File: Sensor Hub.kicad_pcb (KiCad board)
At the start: 4 copper layers, 52.1 x 45.6 mm, 53 parts, among them J1 SWD, J2 SD_Card, J4 USB_B_Micro, Q1 AO3401A, Q2 AO3401A, SW1 SW_SPDT, SW2 SW_Push, U1 LM20BIM7, U2 STM32L100RBT6A_LQFP64, U3 LD_SSOP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

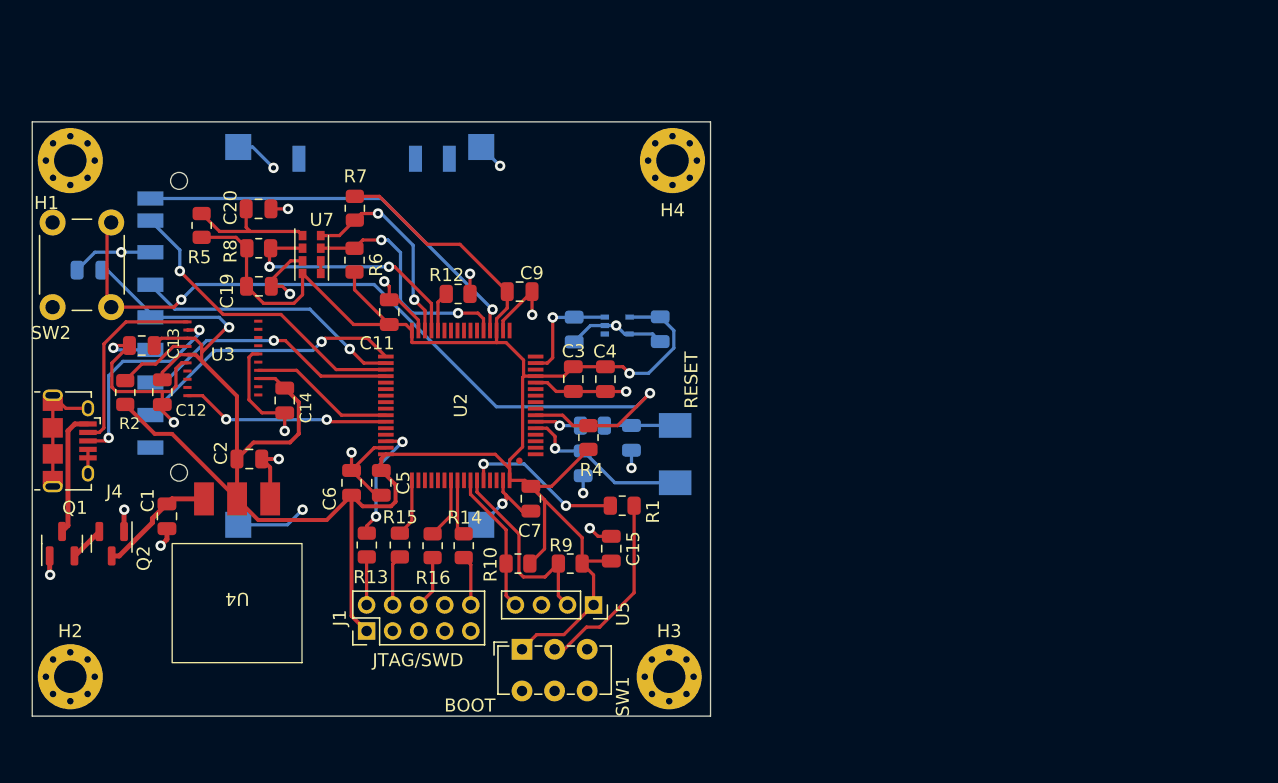
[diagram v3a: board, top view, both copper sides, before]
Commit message: Updated to Rev B
+ Added ESD protection on USB side
+ Redesigned board layout to a SIG/GND/GND/SIG stack up and using L4 as 3V3 plane
+ Resized capacitors and resistors to 0402
+ Added 3D models of certain components
+ Added ferrite bead to 5V line
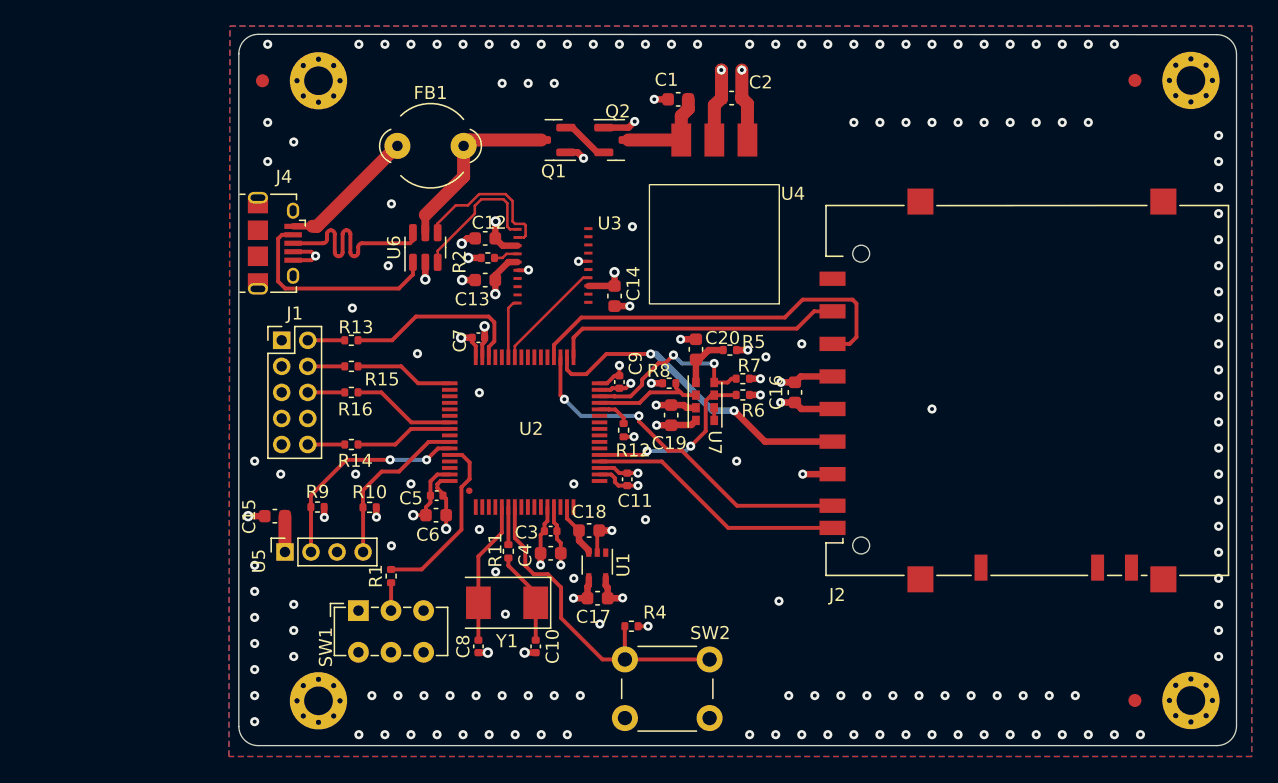
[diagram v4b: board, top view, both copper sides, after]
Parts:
- added FB1: FerriteBead, Ferrite_THT:LairdTech_28C0236-0JW-10, F.Cu at (79.0, 57.8)
- added FID1: Fiducial, Fiducial:Fiducial_1mm_Mask2mm, F.Cu at (68.6, 52.8)
- added FID2: Fiducial, Fiducial:Fiducial_1mm_Mask2mm, F.Cu at (135.6, 100.4)
- added FID3: Fiducial, Fiducial:Fiducial_1mm_Mask2mm, F.Cu at (135.6, 52.8)
- added U6: USBLC6-2SC6, Package_TO_SOT_SMD:SOT-23-6, F.Cu at (81.1, 65.6)
- C1, C12, C13, C14, C15, C19, C2, C20, C4, C6: footprint Capacitor_SMD:C_0805_2012Metric -> Capacitor_SMD:C_0603_1608Metric
- C10, C8: footprint Capacitor_SMD:C_0805_2012Metric -> Capacitor_SMD:C_0402_1005Metric; moved to F.Cu
- C11, C3, C5, C7, C9: footprint Capacitor_SMD:C_0805_2012Metric -> Capacitor_SMD:C_0402_1005Metric
- C16, C17, C18: footprint Capacitor_SMD:C_0805_2012Metric -> Capacitor_SMD:C_0603_1608Metric; moved to F.Cu
- H1, H2, H3, H4: value MountingHole -> MountingHole_Pad; footprint MountingHole:MountingHole_2.5mm_Pad_Via -> MountingHole:MountingHole_2.2mm_M2_Pad_Via
- J2, U1, Y1: moved to F.Cu
- R1, R10, R12, R13, R14, R15, R16, R2, R4, R5, R6, R7, R8, R9: footprint Resistor_SMD:R_0805_2012Metric -> Resistor_SMD:R_0402_1005Metric
- R11: footprint Resistor_SMD:R_0805_2012Metric -> Resistor_SMD:R_0402_1005Metric; moved to F.Cu
- moved H3 60.8 mm to (139.9, 52.8)
- moved H4 57.5 mm to (139.9, 100.4)
- moved C16 55.0 mm to (109.5, 76.7), turned to 90 degrees
- moved J2 52.5 mm to (127.3, 76.6), turned to 90 degrees
- moved SW2 51.8 mm to (96.4, 97.2), turned to 0 degrees
- moved C1 50.6 mm to (100.5, 54.2), turned to 180 degrees
- moved Q2 49.6 mm to (95.7, 57.3), turned to 0 degrees
- moved Q1 48.8 mm to (91.0, 57.3), turned to 180 degrees
- moved C2 46.2 mm to (104.6, 54.1)
- moved U4 45.8 mm to (103.3, 65.2)
- moved R5 41.7 mm to (104.5, 73.5), turned to 0 degrees
- moved C20 35.3 mm to (101.9, 73.4), turned to -90 degrees
- moved R8 33.2 mm to (99.8, 76.0)
- moved C19 33.2 mm to (100.0, 78.5), turned to -90 degrees
- moved R7 32.5 mm to (105.5, 75.7), turned to 0 degrees
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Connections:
- net BOOT0 renamed /BOOT0
- net NJTRST renamed /SWD_NJTRST
- net NRST renamed /NRST
- net OSC_IN renamed /OSC_IN
- net OSC_OUT renamed /OSC_OUT
- net SWCLK renamed /SWD_CLK
- net SWDIO renamed /SWD_IO
- net SWO renamed /SWD_O
- net USART1_RX renamed /USART1_TX
- net USART1_TX renamed /USART1_RX
- H1 pad 1: (no net) -> GND
- H2 pad 1: (no net) -> GND
- H3 pad 1: (no net) -> GND
- H4 pad 1: (no net) -> GND
- J2 pad CP: (no net) -> GND
- J2 pad SW: (no net) -> GND
- J2 pad WP: (no net) -> GND
- J4 pad 1: +5V -> Net-(J4-VBUS)
- J4 pad 2: Net-(J4-D-) -> /USB_D-
- J4 pad 3: Net-(J4-D+) -> /USB_D+
- U3 pad 11: Net-(J4-D-) -> Net-(U3-USB_DP)
- U3 pad 12: Net-(J4-D+) -> Net-(U3-USB_DM)
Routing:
- net +3V3: track 219.8 -> 52.6 mm, vias 2 -> 20
- net GND: track 118.8 -> 59.4 mm, vias 23 -> 172
- net /NRST: track 63.3 -> 25.9 mm, vias 2 -> 0
- net /USB_D-: track 0.00 -> 16.5 mm
- net /USB_D+: track 0.00 -> 16.5 mm
- net Net-(J4-D+): track 16.0 -> 0.00 mm, vias 2 -> 0
- net Net-(J4-D-): track 14.9 -> 0.00 mm
- net Net-(SW1-B): track 14.6 -> 2.14 mm
- net Net-(U3-USB_DM): track 0.00 -> 11.8 mm
- net SPI1_IRQ: track 31.5 -> 20.0 mm, vias 1 -> 0
- net /USART1_TX: track 16.1 -> 4.64 mm, vias 2 -> 0
- net Net-(U3-USB_DP): track 0.00 -> 11.0 mm
- net I2C2_CLK: track 19.6 -> 8.68 mm, vias 2 -> 0
- net Net-(J4-VBUS): track 0.00 -> 10.6 mm
- net SPI1_MOSI: track 20.5 -> 30.4 mm, vias 1 -> 0
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- added copper zone on B.Cu, net +3V3
- added copper zone on F.Cu, net GND
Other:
- board size 52.1 x 45.6 mm -> 76.6 x 54.6 mm
- board text removed: "BOOT"
- board text removed: "JTAG/SWD"
- board text removed: "RESET"
